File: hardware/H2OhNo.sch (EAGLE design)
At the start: 13 parts, among them U2 TINY85-20-DIP

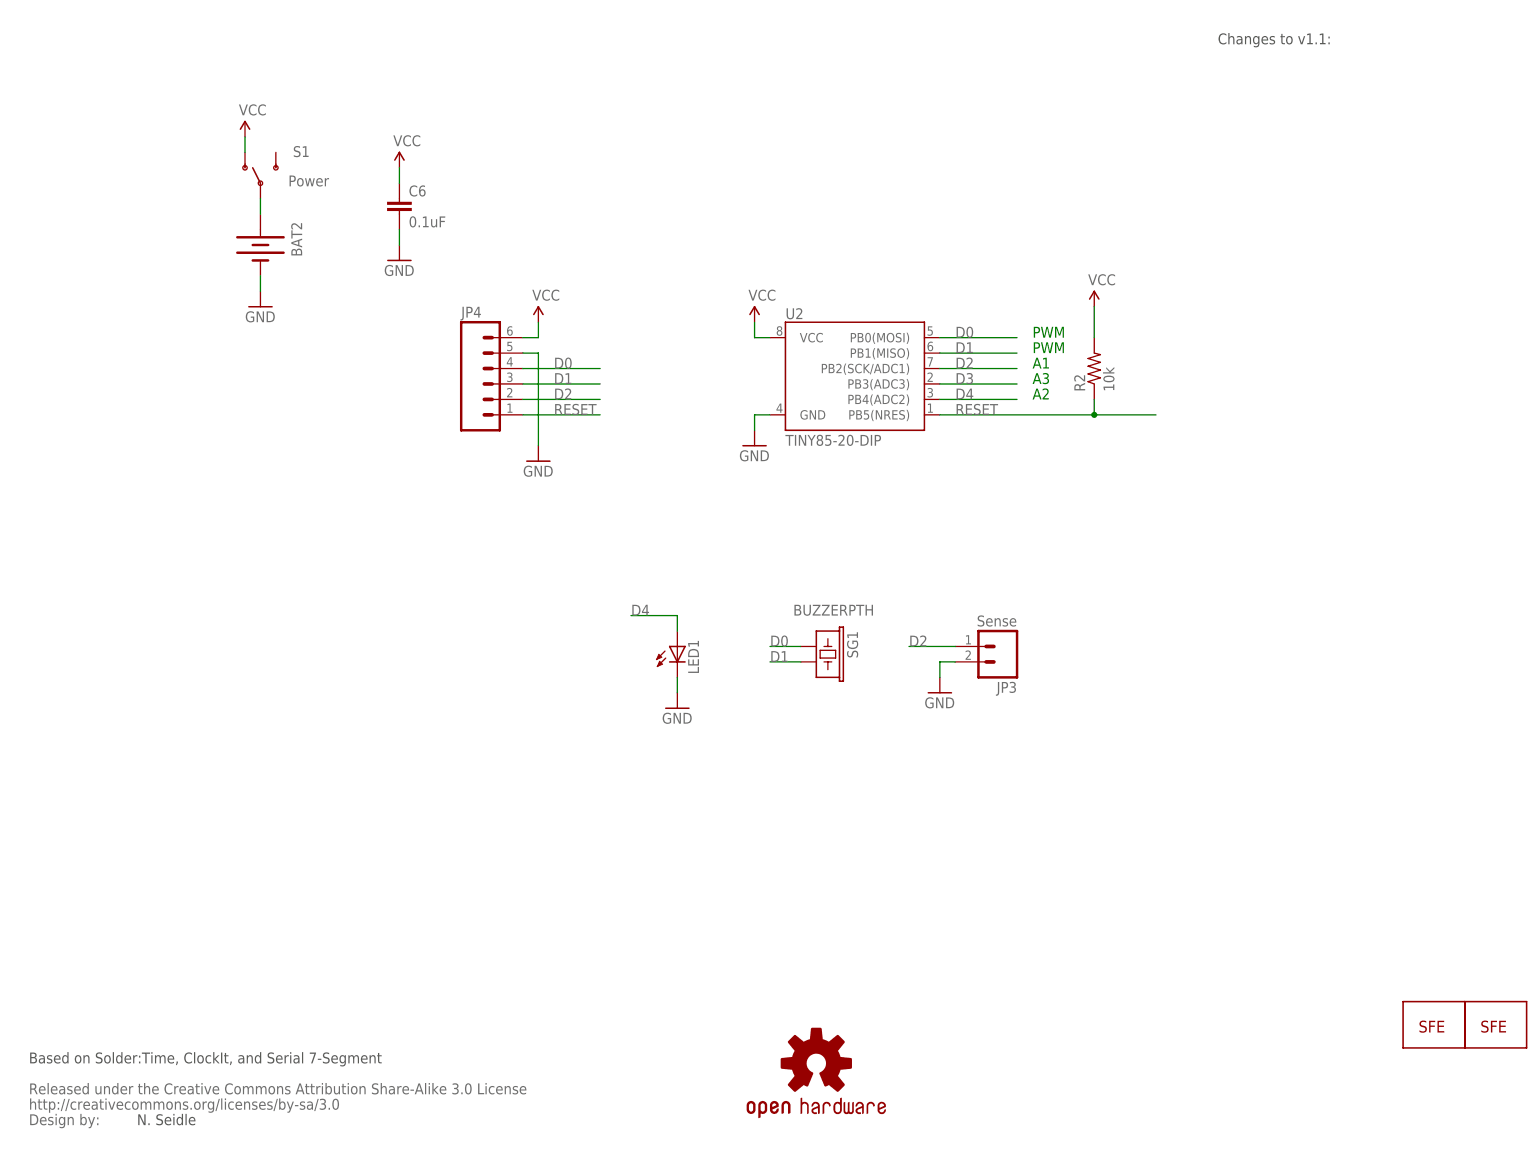
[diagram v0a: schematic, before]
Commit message: Added version #. Fixed file naming. Removed 10k on RES.
Fixed footprint on CR2032 as well.
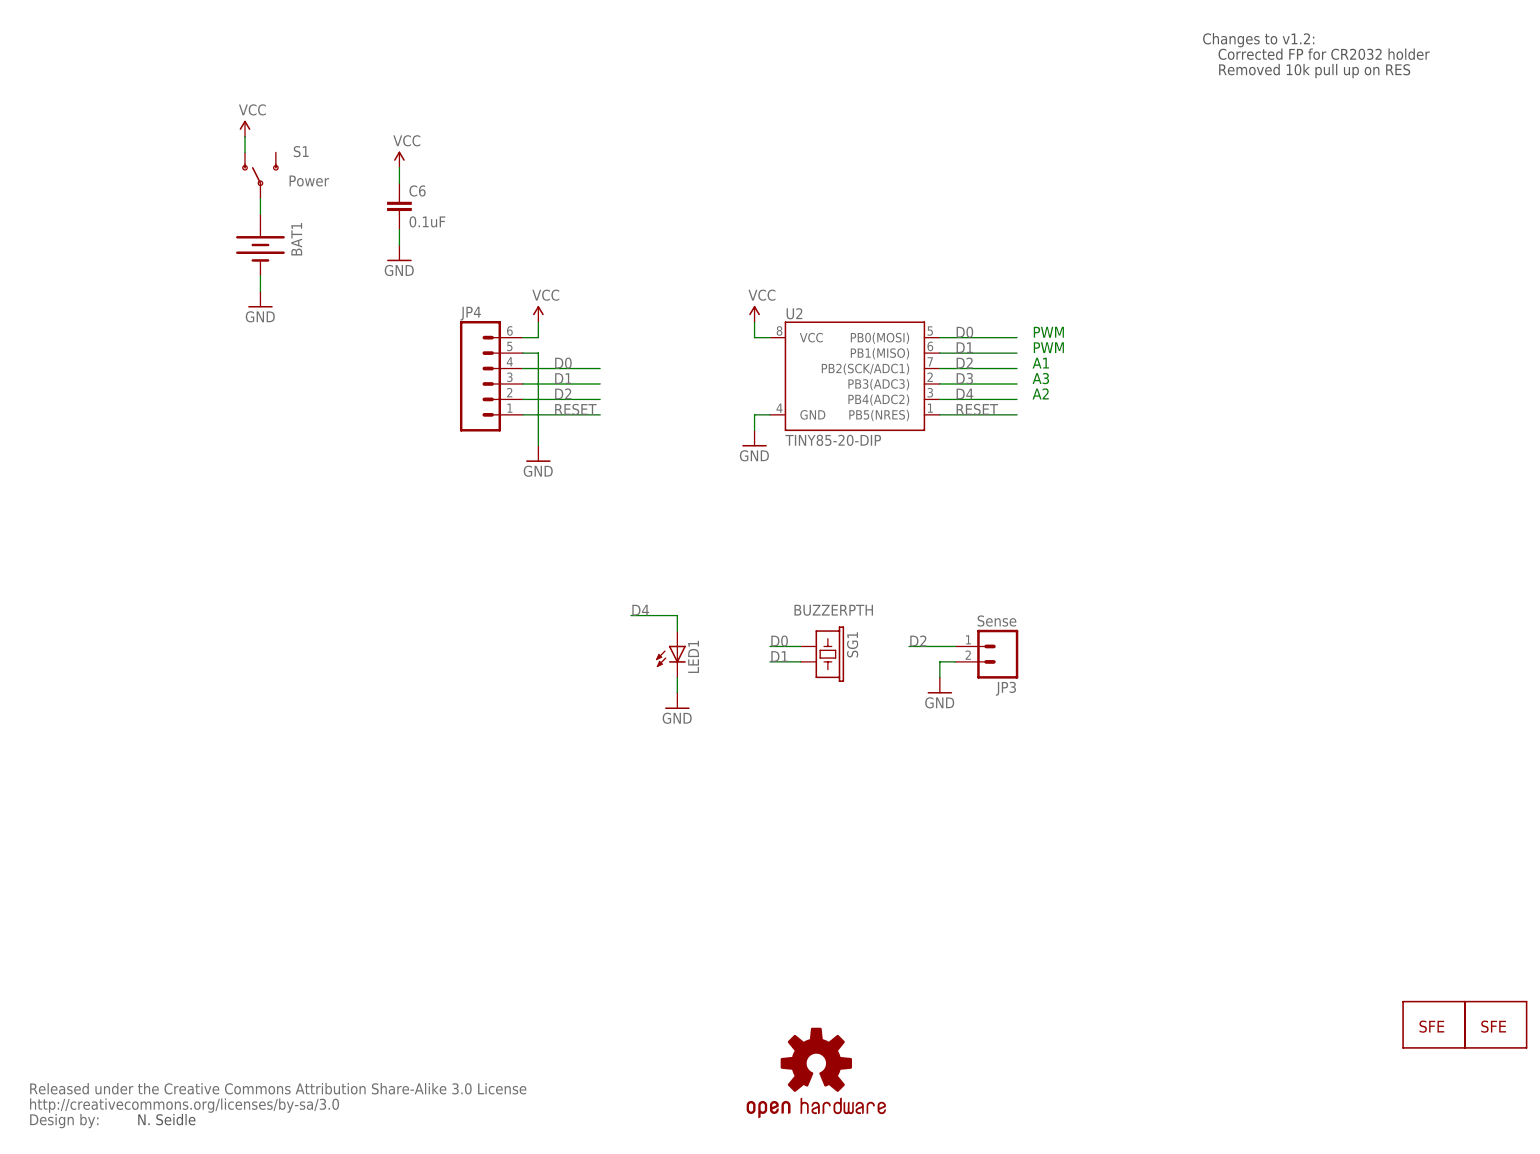
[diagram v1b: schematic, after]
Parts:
- removed BAT2: (no value), Testing:BATTERY20PTH
- removed R2: 10k, SparkFun:RESISTORAXIAL-0.3
- added BAT1: (no value), SparkFun-Electromechanical:BATTERY20PTH
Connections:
- net GND: now also BAT1.-; no longer BAT2.-
- net N$1: now also BAT1.+; no longer BAT2.+
- net RESET: no longer R2.1
- net VCC: no longer R2.2
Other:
- note added: "Changes to v1.2:"
- note added: "Corrected FP for CR2032 holder"
- note added: "Removed 10k pull up on RES"
- note removed: "Based on Solder:Time, ClockIt, and Serial 7-Segment"
- note removed: "Changes to v1.1:"

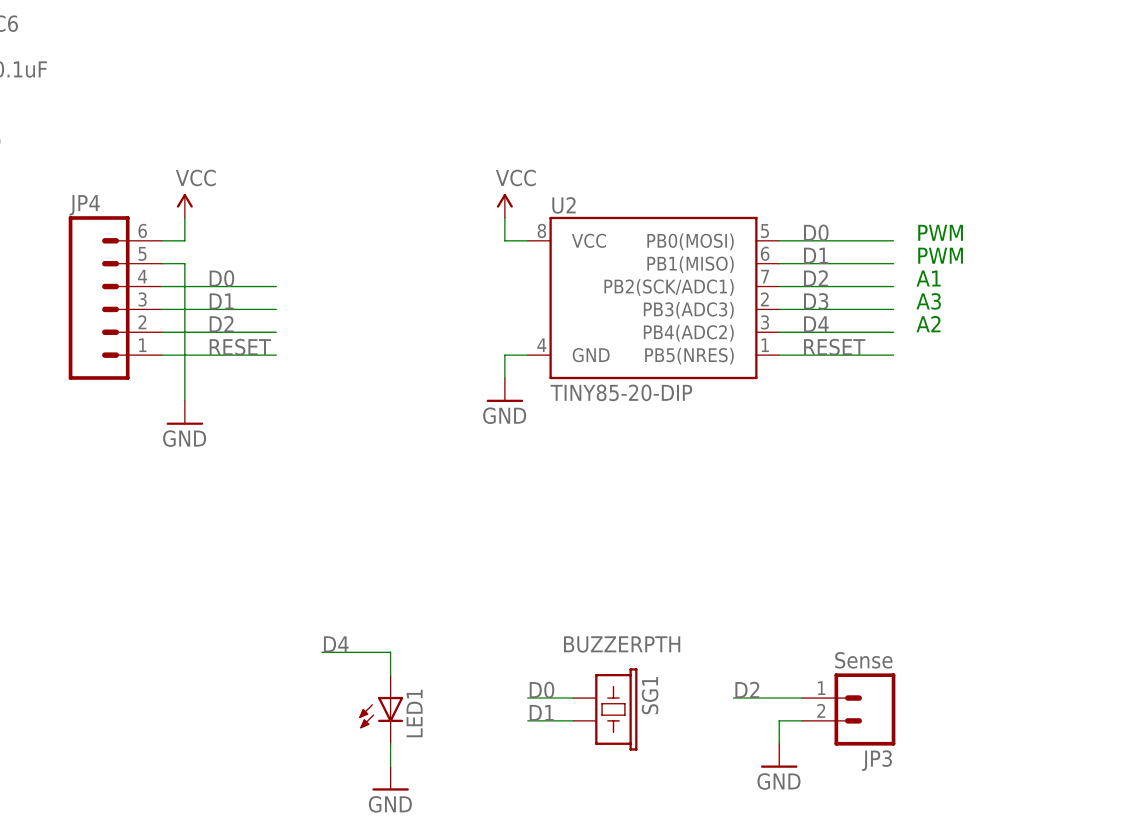
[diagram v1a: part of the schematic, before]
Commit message: Modified 6-pin SIP header for FTDI compatibility
It's not serial, but you should be able to bit-bang serial out the
MOSI/MISO lines and use an FTDI on the programming header. Good for
debugging.
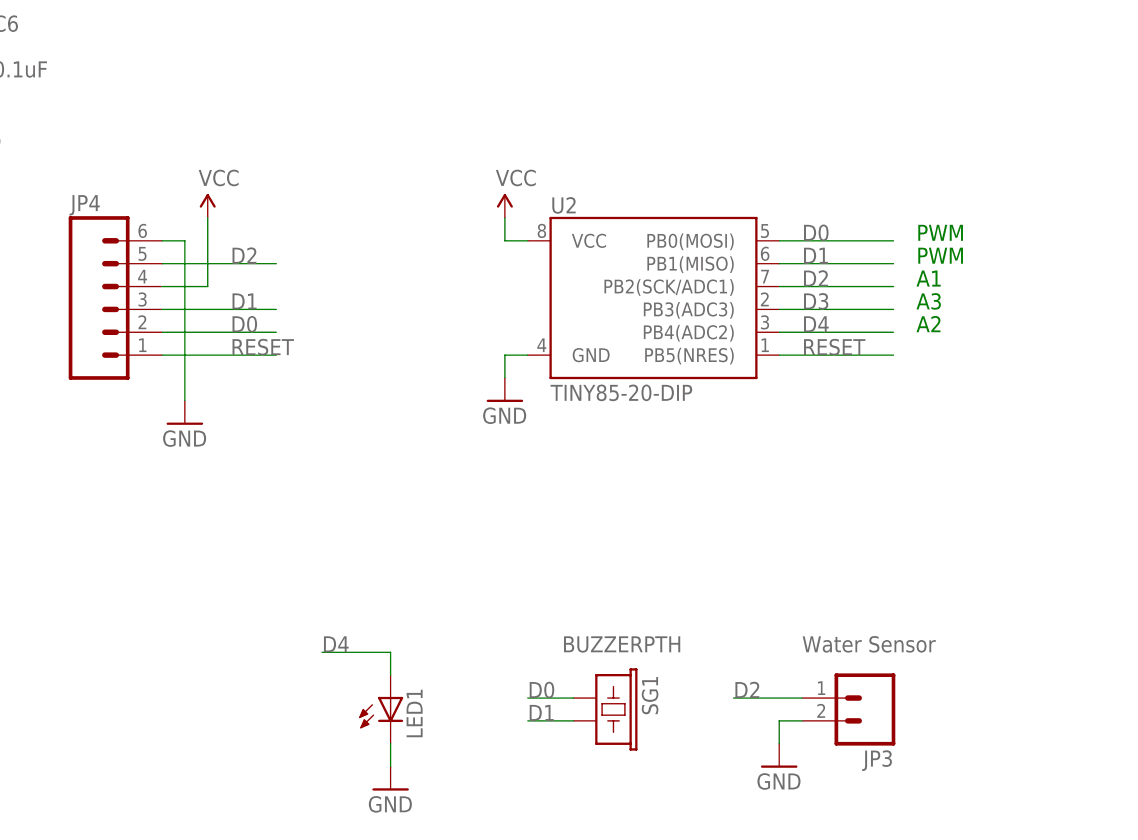
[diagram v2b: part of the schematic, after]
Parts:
- JP3: value Sense -> Water Sensor
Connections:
- net D0: now also JP4.2; no longer JP4.4
- net D2: now also JP4.5; no longer JP4.2
- net GND: now also JP4.6; no longer JP4.5
- net VCC: now also JP4.4; no longer JP4.6
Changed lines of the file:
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@@
 <attribute name="VALUE" value="TINY85-20-DIP"/>
 </part>
-<part name="JP3" library="SparkFun-Connectors" deviceset="M02" device="PTH" value="Sense"/>
+<part name="JP3" library="SparkFun-Connectors" deviceset="M02" device="PTH" value="Water Sensor"/>
 <part name="LED1" library="SparkFun-LED" deviceset="LED" device="5MM"/>
 <part name="SG1" library="SparkFun-Electromechanical" deviceset="BUZZER" device="PTH"/>
@@
 <attribute name="NAME" x="127" y="135.128" size="1.778" layer="95"/>
 </instance>
-<instance part="JP3" gate="G$1" x="162.56" y="81.28" rot="R180"/>
+<instance part="JP3" gate="G$1" x="162.56" y="81.28" smashed="yes" rot="R180">
+<attribute name="VALUE" x="154.94" y="86.36" size="1.778" layer="96"/>
+<attribute name="NAME" x="165.1" y="75.438" size="1.778" layer="95" rot="R180"/>
+</instance>
 <instance part="LED1" gate="G$1" x="109.22" y="81.28"/>
 <instance part="SG1" gate="G$1" x="132.08" y="81.28" smashed="yes" rot="R270">
@@
 </instance>
 <instance part="JP4" gate="G$1" x="78.74" y="124.46"/>
-<instance part="P+4" gate="1" x="86.36" y="134.62"/>
+<instance part="P+4" gate="1" x="88.9" y="134.62"/>
 <instance part="P+5" gate="1" x="121.92" y="134.62"/>
 <instance part="GND1" gate="1" x="86.36" y="111.76"/>
@@
 </segment>
 <segment>
-<pinref part="JP4" gate="G$1" pin="5"/>
-<wire x1="83.82" y1="129.54" x2="86.36" y2="129.54" width="0.1524" layer="91"/>
-<wire x1="86.36" y1="129.54" x2="86.36" y2="114.3" width="0.1524" layer="91"/>
+<wire x1="86.36" y1="132.08" x2="86.36" y2="114.3" width="0.1524" layer="91"/>
 <pinref part="GND1" gate="1" pin="GND"/>
+<pinref part="JP4" gate="G$1" pin="6"/>
+<wire x1="83.82" y1="132.08" x2="86.36" y2="132.08" width="0.1524" layer="91"/>
 </segment>
 <segment>
@@
 </segment>
 <segment>
-<pinref part="JP4" gate="G$1" pin="6"/>
-<wire x1="83.82" y1="132.08" x2="86.36" y2="132.08" width="0.1524" layer="91"/>
-<wire x1="86.36" y1="132.08" x2="86.36" y2="134.62" width="0.1524" layer="91"/>
-<pinref part="P+4" gate="1" pin="VCC"/>
-</segment>
-<segment>
 <pinref part="U2" gate="G$1" pin="VCC"/>
 <pinref part="P+5" gate="1" pin="VCC"/>
@@
 <wire x1="38.1" y1="165.1" x2="38.1" y2="162.56" width="0.1524" layer="91"/>
 </segment>
+<segment>
+<pinref part="JP4" gate="G$1" pin="4"/>
+<pinref part="P+4" gate="1" pin="VCC"/>
+<wire x1="83.82" y1="127" x2="88.9" y2="127" width="0.1524" layer="91"/>
+<wire x1="88.9" y1="127" x2="88.9" y2="134.62" width="0.1524" layer="91"/>
+</segment>
 </net>
 <net name="RESET" class="0">
@@
 <pinref part="JP4" gate="G$1" pin="1"/>
 <wire x1="83.82" y1="119.38" x2="96.52" y2="119.38" width="0.1524" layer="91"/>
-<label x="88.9" y="119.38" size="1.778" layer="95"/>
+<label x="91.44" y="119.38" size="1.778" layer="95"/>
 </segment>
 </net>
@@
 <net name="D0" class="0">
 <segment>
-<pinref part="JP4" gate="G$1" pin="4"/>
-<wire x1="83.82" y1="127" x2="96.52" y2="127" width="0.1524" layer="91"/>
-<label x="88.9" y="127" size="1.778" layer="95"/>
-</segment>
-<segment>
 <pinref part="U2" gate="G$1" pin="PB0(MOSI)"/>
 <wire x1="152.4" y1="132.08" x2="165.1" y2="132.08" width="0.1524" layer="91"/>
@@
 <label x="124.46" y="81.28" size="1.778" layer="95"/>
 </segment>
+<segment>
+<pinref part="JP4" gate="G$1" pin="2"/>
+<wire x1="83.82" y1="121.92" x2="96.52" y2="121.92" width="0.1524" layer="91"/>
+<label x="91.44" y="121.92" size="1.778" layer="95"/>
+</segment>
 </net>
 <net name="D1" class="0">
-<segment>
-<pinref part="JP4" gate="G$1" pin="3"/>
-<wire x1="83.82" y1="124.46" x2="96.52" y2="124.46" width="0.1524" layer="91"/>
-<label x="88.9" y="124.46" size="1.778" layer="95"/>
-</segment>
 <segment>
 <pinref part="U2" gate="G$1" pin="PB1(MISO)"/>
@@
 <label x="124.46" y="78.74" size="1.778" layer="95"/>
 </segment>
+<segment>
+<pinref part="JP4" gate="G$1" pin="3"/>
+<wire x1="83.82" y1="124.46" x2="96.52" y2="124.46" width="0.1524" layer="91"/>
+<label x="91.44" y="124.46" size="1.778" layer="95"/>
+</segment>
 </net>
 <net name="D2" class="0">
-<segment>
-<pinref part="JP4" gate="G$1" pin="2"/>
-<wire x1="83.82" y1="121.92" x2="96.52" y2="121.92" width="0.1524" layer="91"/>
-<label x="88.9" y="121.92" size="1.778" layer="95"/>
-</segment>
 <segment>
 <pinref part="U2" gate="G$1" pin="PB2(SCK/ADC1)"/>
@@
 <label x="147.32" y="81.28" size="1.778" layer="95"/>
 </segment>
-</net>
+<segment>
+<pinref part="JP4" gate="G$1" pin="5"/>
+<wire x1="83.82" y1="129.54" x2="96.52" y2="129.54" width="0.1524" layer="91"/>
+<label x="91.44" y="129.54" size="1.778" layer="95"/>
+</segment>
+</net>
